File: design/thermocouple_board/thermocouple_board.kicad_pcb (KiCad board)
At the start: 2 copper layers, 73.9 x 56.6 mm, 68 parts, among them J1 Prog Conn, J2 CAN Conn, J3 CAN Ext Conn, J4 Thermocouple conn, J5 Thermocouple conn, J6 Thermocouple conn, J7 Thermocouple conn, U1 PIC18LF26K83, U2 MCP2562, U3 AP2120N-3.3TRG1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

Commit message: Finished routing, still need to add logo
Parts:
- moved R4 23.9 mm to (137.8, 124.7), turned to 180 degrees
- moved L5 2.97 mm to (146.9, 86.5)
- moved J7 2.75 mm to (154.3, 78.7)
- moved J4 2.75 mm to (116.2, 78.7)
- moved J5 2.75 mm to (128.9, 78.7)
- moved J6 2.75 mm to (141.6, 78.7)
- moved L1 2.58 mm to (121.4, 86.5)
- moved L2 2.58 mm to (116.1, 86.5)
- moved L4 2.58 mm to (128.8, 86.5)
- moved L3 2.58 mm to (134.1, 86.5)
- moved L7 2.58 mm to (159.9, 86.5)
- moved L6 2.09 mm to (141.6, 86.5)
- moved L8 1.62 mm to (154.4, 86.5)
- moved H2 1.59 mm to (170.8, 75.6)
- moved C5 0.89 mm to (149.6, 124.7)
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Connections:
- J3 pad 1: +5V -> GND
- J3 pad 2: /CANH -> /CANL
- J3 pad 3: /CANL -> /CANH
- J3 pad 4: GND -> +5V
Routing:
- net GND: track 0.00 -> 155.6 mm, vias 0 -> 10
- net /CANH: track 0.00 -> 108.0 mm
- net +5V: track 0.00 -> 102.7 mm, vias 0 -> 2
- net /CANL: track 0.00 -> 87.8 mm
- net +3.3V: track 0.00 -> 82.5 mm, vias 0 -> 9
- net SCLK: track 0.00 -> 77.9 mm, vias 0 -> 4
- net MISO: track 0.00 -> 72.4 mm, vias 0 -> 2
- net /CAN_RX: track 0.00 -> 69.9 mm, vias 0 -> 2
- net /CAN_TX: track 0.00 -> 53.0 mm, vias 0 -> 2
- net /CS4: track 0.00 -> 40.7 mm
- net /CS1: track 0.00 -> 36.0 mm
- net /~{MCLR}: track 0.00 -> 34.8 mm
- net /CS3: track 0.00 -> 34.3 mm
- net /CS2: track 0.00 -> 32.8 mm
- net /ICSPDAT: track 0.00 -> 22.6 mm
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- added copper zone on F.Cu, net +3.3V
- added copper zone on B.Cu, net GND
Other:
- outline, holes or cut-outs redrawn
- board text added: "3.3V"
- board text added: "5V"

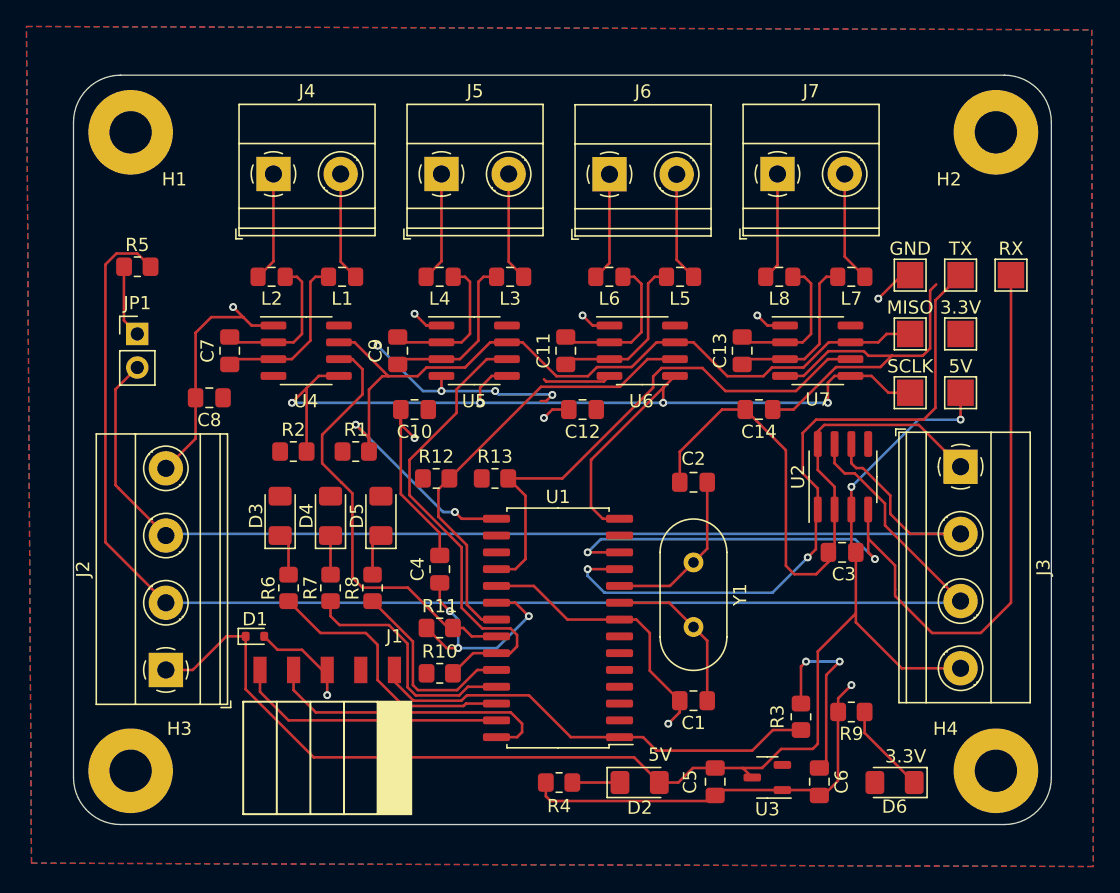
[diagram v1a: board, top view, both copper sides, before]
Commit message: Finished board routing
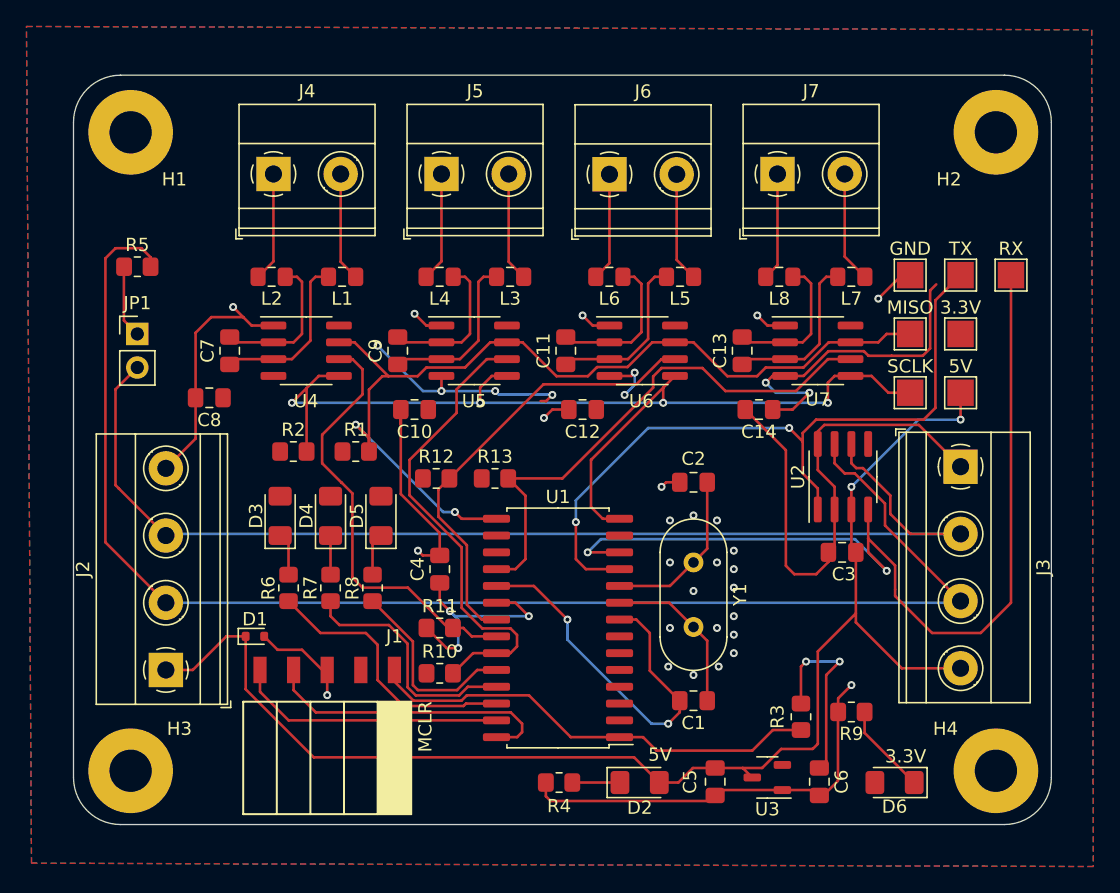
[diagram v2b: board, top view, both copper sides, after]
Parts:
- added G***: LOGO, rlcs:rocketry_logo_small, B.Cu at (129.2, 121.7)
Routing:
- net +3.3V: track 82.5 -> 79.0 mm, vias 9 -> 13
- net /CAN_TX: track 53.0 -> 56.0 mm
- net /CAN_RX: track 69.9 -> 72.5 mm
- net GND: track 155.6 -> 156.7 mm, vias 10 -> 29
- net /CANH: track 108.0 -> 109.0 mm
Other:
- board text added: "MCLR"
- board text added: "Thermocouple Board Mar 2024 Domenic Hampson"

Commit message: Addressed comments
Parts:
- removed the G*** at (129.2, 121.7)
- added G***: LOGO, logo:Logo_SilkScreen_10mm, B.Cu at (128.3, 121.2)
- +3.3V: renamed from 3.3V; footprint TestPoint:TestPoint_Pad_2.0x2.0mm -> TestPoint:TestPoint_Keystone_5005-5009_Compact
- +5V: renamed from 5V; footprint TestPoint:TestPoint_Pad_2.0x2.0mm -> TestPoint:TestPoint_Keystone_5005-5009_Compact
- GND, MISO, RX, SCLK, TX: footprint TestPoint:TestPoint_Pad_2.0x2.0mm -> TestPoint:TestPoint_Keystone_5005-5009_Compact
- moved J3 15.2 mm to (168.1, 116.1), turned to 90 degrees
- moved J2 15.2 mm to (108.1, 101.0), turned to -90 degrees
- moved GND 8.91 mm to (165.0, 77.5)
- moved +5V 7.05 mm to (169.8, 88.4)
- moved SCLK 5.64 mm to (169.8, 93.9)
- moved J6 5.12 mm to (146.7, 78.1), turned to 180 degrees
- moved J5 5.12 mm to (134.0, 78.1), turned to 180 degrees
- moved J4 5.12 mm to (121.3, 78.1), turned to 180 degrees
- moved J7 5.12 mm to (159.4, 78.1), turned to 180 degrees
- moved TX 4.67 mm to (165.0, 82.9)
- moved RX 4.05 mm to (169.8, 82.9)
- moved +3.3V 3.99 mm to (165.0, 88.4)
- moved MISO 3.11 mm to (165.0, 93.9)
- moved R9 1.81 mm to (161.3, 120.5)
- moved D1 0.76 mm to (115.6, 113.7)
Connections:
- J2 pad 1: +5V -> GND
- J2 pad 2: /CANH -> /CANL
- J2 pad 3: /CANL -> /CANH
- J2 pad 4: GND -> +5V
- J3 pad 1: GND -> +5V
- J3 pad 2: /CANL -> /CANH
- J3 pad 3: /CANH -> /CANL
- J3 pad 4: +5V -> GND
- L1 pad 1: Net-(J4-Pin_2) -> Net-(J4-Pin_1)
- L2 pad 1: Net-(J4-Pin_1) -> Net-(J4-Pin_2)
- L3 pad 1: Net-(J5-Pin_2) -> Net-(J5-Pin_1)
- L4 pad 1: Net-(J5-Pin_1) -> Net-(J5-Pin_2)
- L5 pad 1: Net-(J6-Pin_2) -> Net-(J6-Pin_1)
- L6 pad 1: Net-(J6-Pin_1) -> Net-(J6-Pin_2)
- L7 pad 1: Net-(J7-Pin_2) -> Net-(J7-Pin_1)
- L8 pad 1: Net-(J7-Pin_1) -> Net-(J7-Pin_2)
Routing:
- net +5V: track 102.7 -> 115.1 mm
- net /CAN_TX: track 56.0 -> 67.5 mm
- net GND: track 156.7 -> 147.5 mm, vias 29 -> 28
- net SCLK: track 77.9 -> 84.8 mm
- net /CAN_RX: track 72.5 -> 77.2 mm, vias 2 -> 4
- net /CS4: track 40.7 -> 42.5 mm
- net MISO: track 72.4 -> 73.8 mm
- net Net-(D6-K): track 6.89 -> 5.77 mm
- net Net-(J7-Pin_1): track 8.14 -> 9.01 mm
- net Net-(J6-Pin_1): track 8.18 -> 8.91 mm
- net +3.3V: track 79.0 -> 78.3 mm
- net Net-(J5-Pin_2): track 8.24 -> 8.86 mm
- net Net-(J4-Pin_2): track 8.24 -> 8.86 mm
- net Net-(J4-Pin_1): track 8.25 -> 8.85 mm
- net Net-(J5-Pin_1): track 8.25 -> 8.85 mm
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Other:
- board text added: "~{MCLR}"
- board text removed: "MCLR"
